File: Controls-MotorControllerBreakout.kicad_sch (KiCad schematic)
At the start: 12 parts, among them J1 MC CAN 1, J2 MC CAN 2, J3 Controls CAN, J4 CANdapter, J5 Ext. PWR

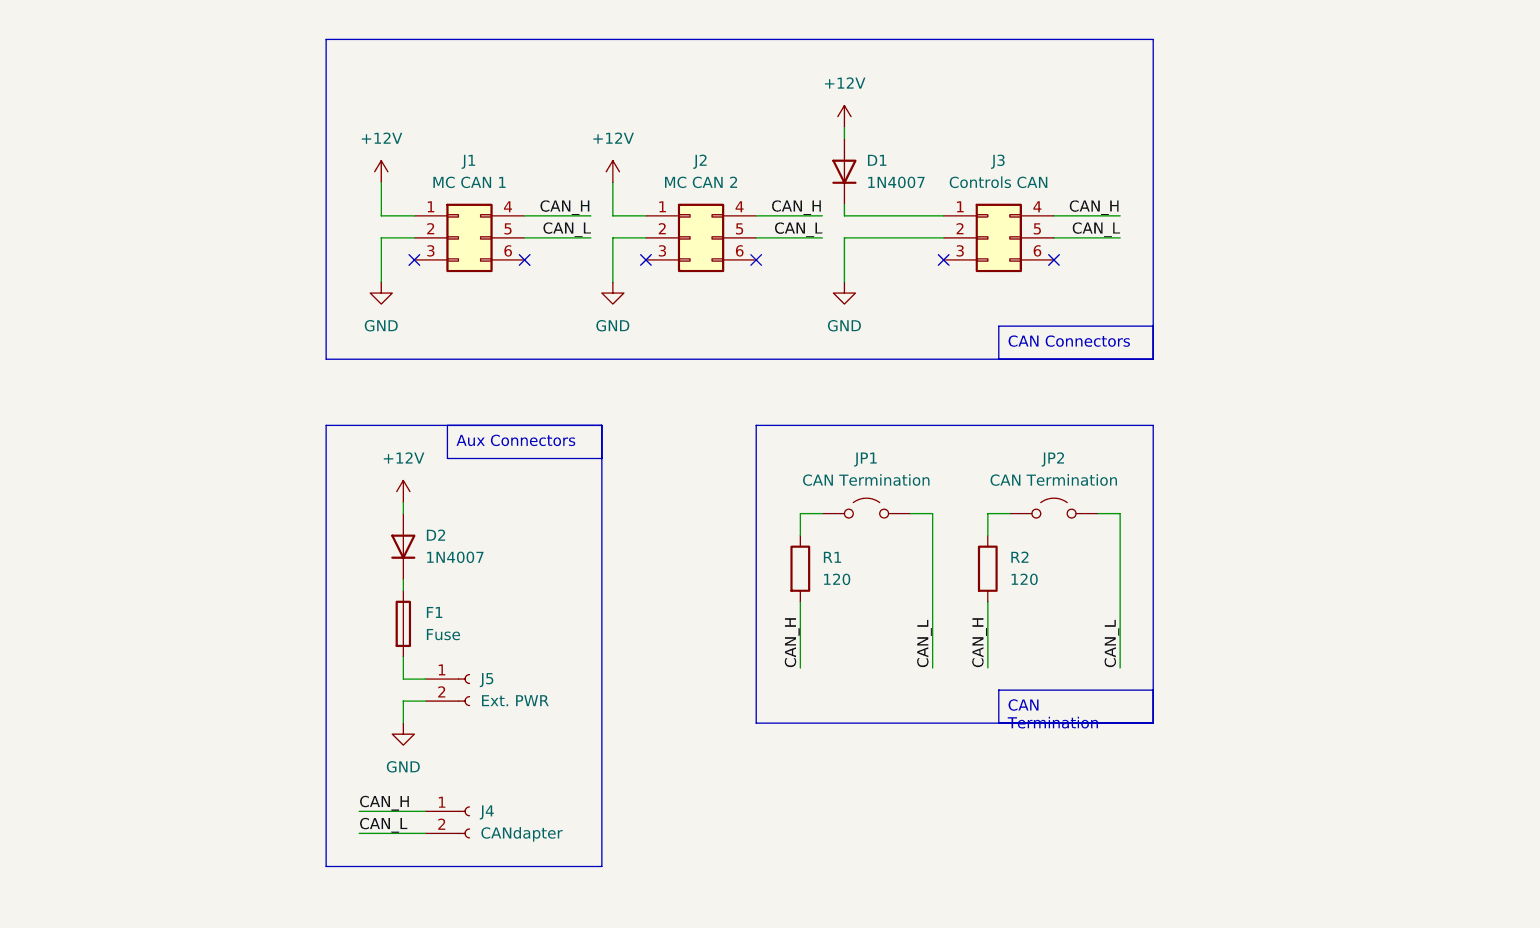
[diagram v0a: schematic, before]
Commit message: add alternative controls conn
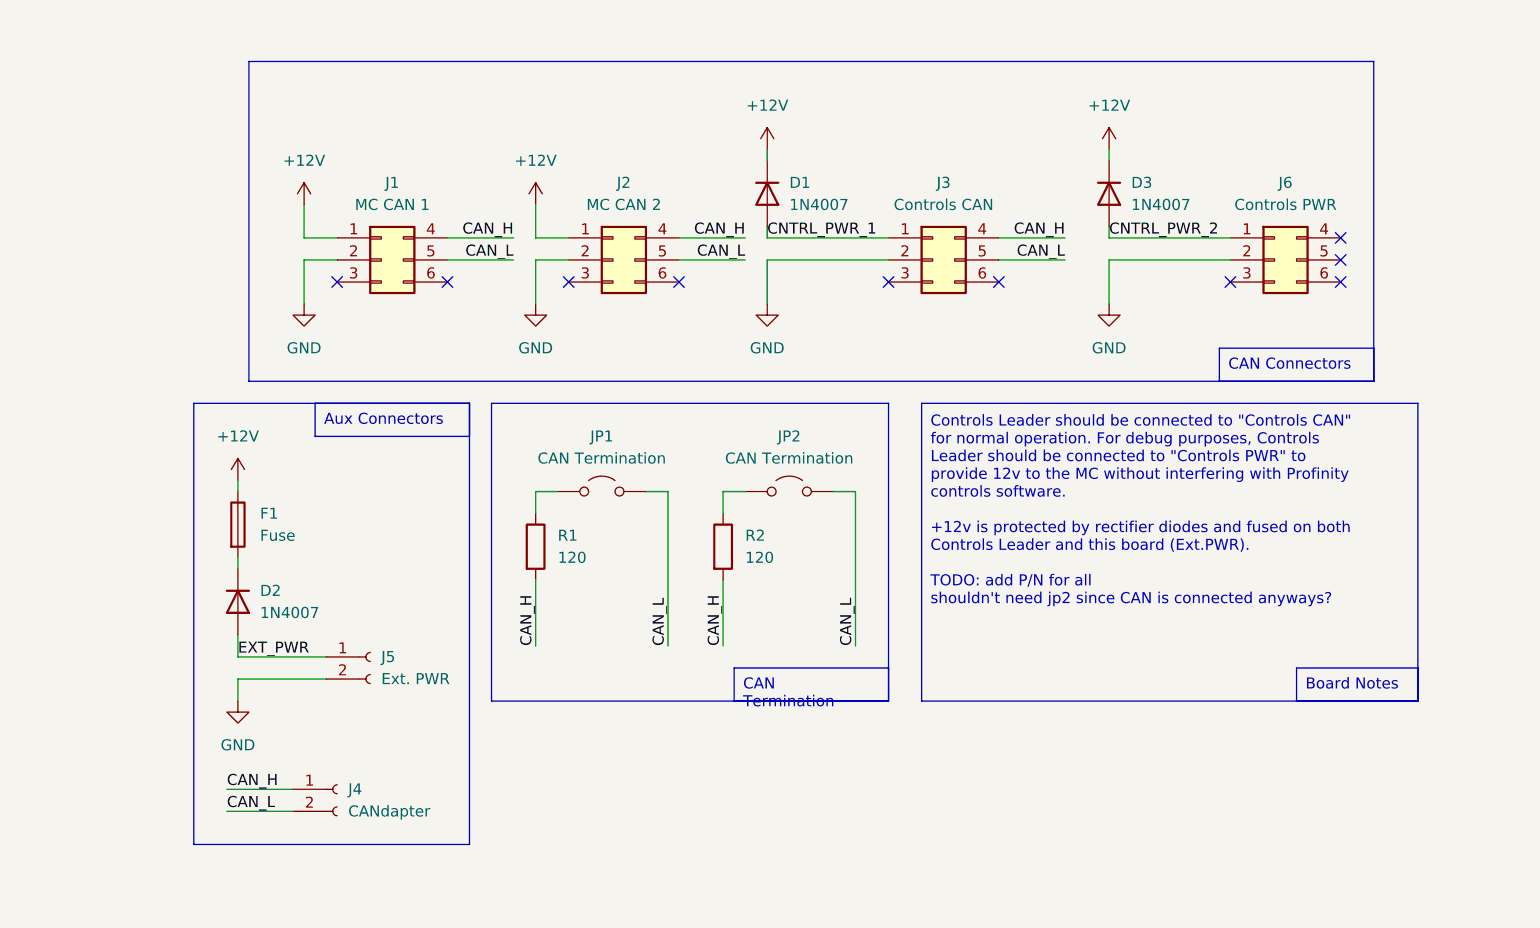
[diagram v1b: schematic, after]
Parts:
- added D3: 1N4007, Diode_SMD:D_SOD-123F, symbol Device:D
- added J6: Controls PWR, Connector_Molex:Molex_Micro-Fit_3.0_43045-0612_2x03_P3.00mm_Vertical, symbol Connector_Generic:Conn_02x03_Top_Bottom
- D1, D2: footprint (none) -> Diode_SMD:D_SOD-123F
- J1, J2, J3: footprint (none) -> Connector_Molex:Molex_Micro-Fit_3.0_43045-0612_2x03_P3.00mm_Vertical
- J4, J5: footprint (none) -> Connector_Molex:Molex_Micro-Fit_3.0_43650-0215_1x02_P3.00mm_Vertical
- JP1, JP2: footprint (none) -> Connector_PinHeader_2.54mm:PinHeader_1x02_P2.54mm_Vertical
- R1, R2: footprint (none) -> Resistor_SMD:R_0805_2012Metric
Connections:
- net +12V: now also D1.1 (K), F1.1, D3.1 (K); no longer D1.2 (A), D2.2 (A)
- net GND: now also J6.2 (Pin_2)
- net at D2.1 (K): now also F1.2; no longer F1.1
- net EXT_PWR: now reaches J5.1 (Pin_1)
- net EXT_PWR: now also D2.2 (A); no longer F1.2
- net CNTRL_PWR_1: now reaches J3.1 (Pin_1)
- net CNTRL_PWR_1: now also D1.2 (A); no longer D1.1 (K)
- new net CNTRL_PWR_2: D3.2 (A), J6.1 (Pin_1)
- no-connect marks 6 -> 10
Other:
- note added: "Controls Leader should be connected to "Controls CAN" for normal operation. For debug purposes, Controls Leader should be connected to "Controls PWR" to provide 12v to the MC without interfering with Profinity controls software. +12v is protected by rectifier diodes and fused on both Controls Leader and this board (Ext.PWR). TODO: add P/N for all shouldn't need jp2 since CAN is connected anyways?"
- moved on the sheet: D1, J1, J2, J3, J4, J5, JP1, JP2, R1, R2

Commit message: decouple pwr from can
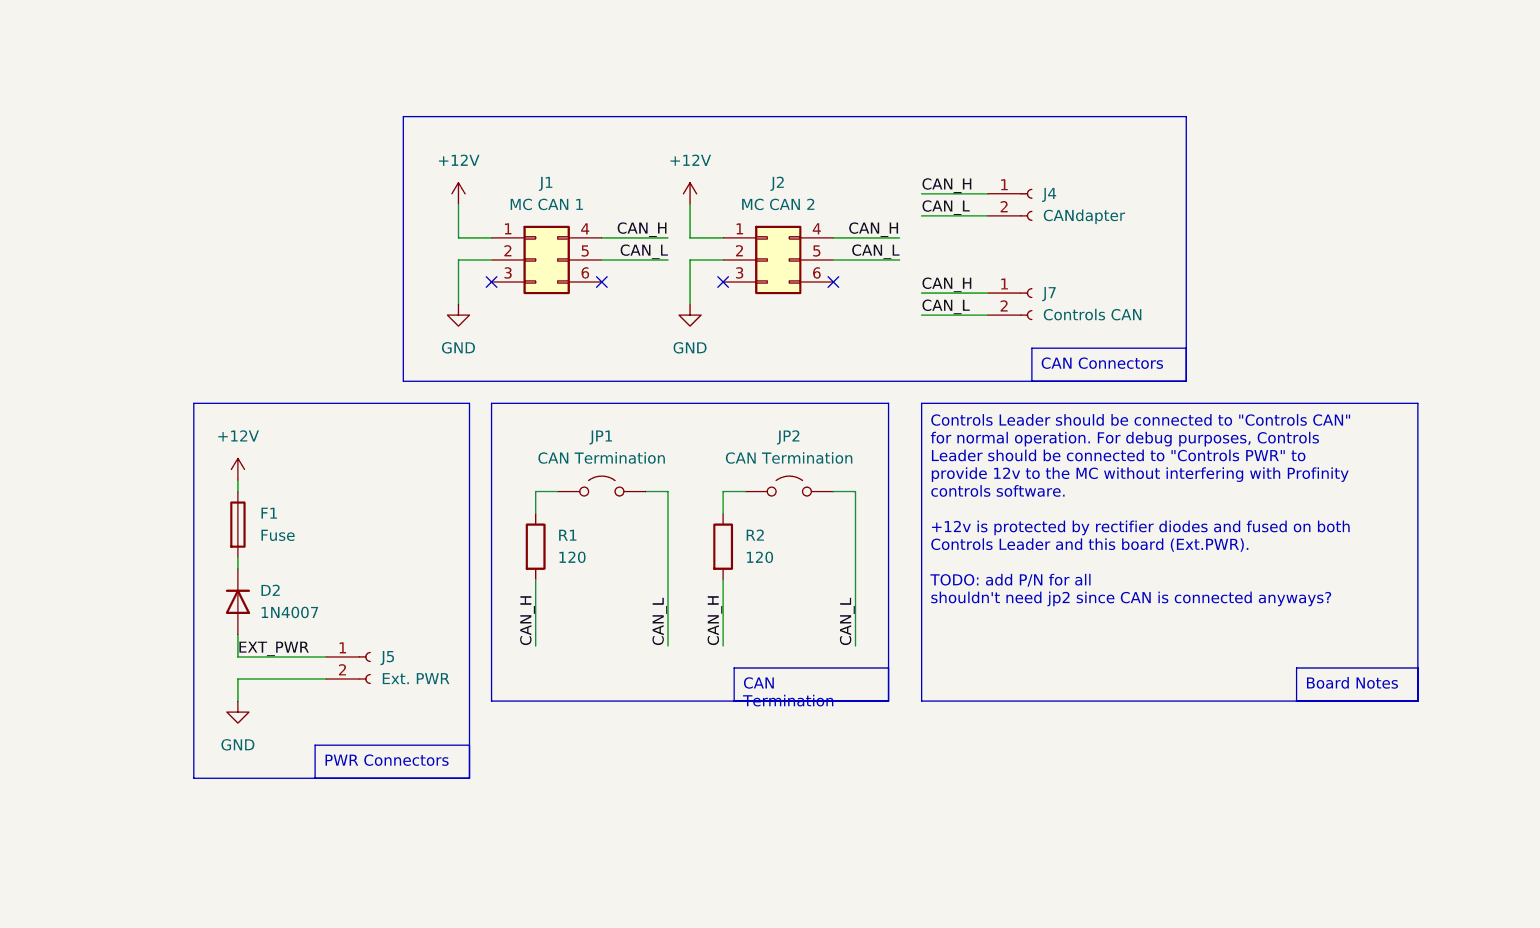
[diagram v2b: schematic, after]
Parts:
- removed D1, D3: 1N4007, Diode_SMD:D_SOD-123F, symbol Device:D
- removed J3: Controls CAN, Connector_Molex:Molex_Micro-Fit_3.0_43045-0612_2x03_P3.00mm_Vertical, symbol Connector_Generic:Conn_02x03_Top_Bottom
- removed J6: Controls PWR, Connector_Molex:Molex_Micro-Fit_3.0_43045-0612_2x03_P3.00mm_Vertical, symbol Connector_Generic:Conn_02x03_Top_Bottom
- added J7: Controls CAN, Connector_Molex:Molex_Micro-Fit_3.0_43650-0215_1x02_P3.00mm_Vertical, symbol Connector:Conn_01x02_Socket
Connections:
- net CAN_H: now also J7.1 (Pin_1)
- net CAN_L: now also J7.2 (Pin_2)
- no-connect marks 10 -> 4
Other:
- moved on the sheet: J1, J2

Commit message: pwr led and rm second term resistors
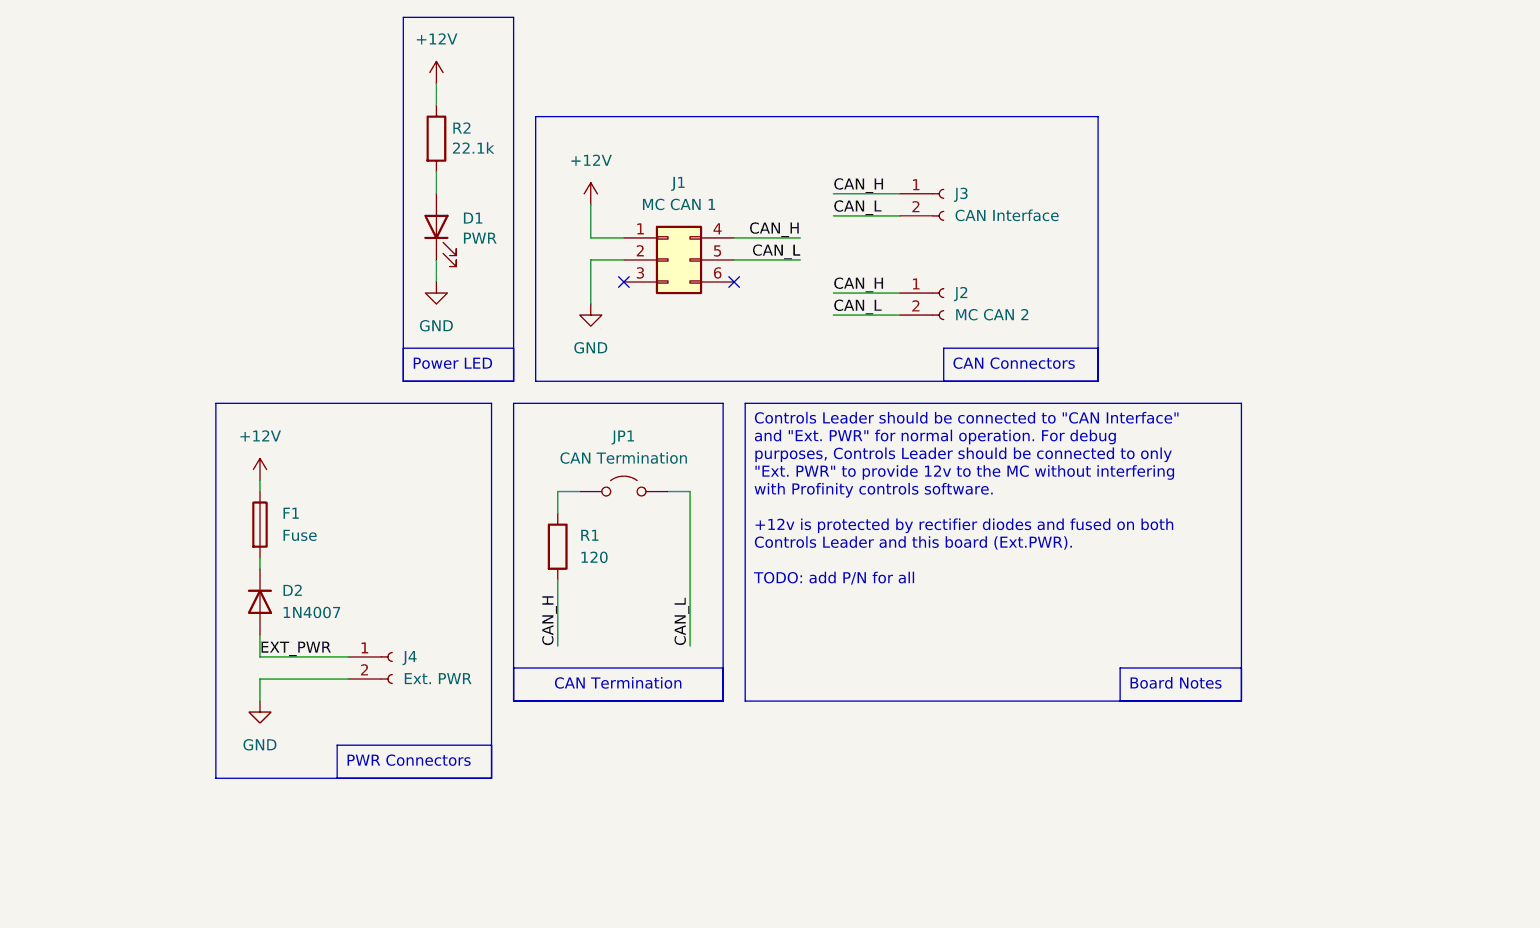
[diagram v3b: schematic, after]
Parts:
- removed J2: MC CAN 2, Connector_Molex:Molex_Micro-Fit_3.0_43045-0612_2x03_P3.00mm_Vertical, symbol Connector_Generic:Conn_02x03_Top_Bottom
- removed JP2: CAN Termination, Connector_PinHeader_2.54mm:PinHeader_1x02_P2.54mm_Vertical, symbol Jumper:Jumper_2_Open
- added D1: PWR, LED_SMD:LED_0805_2012Metric, symbol Device:LED
- J2: renamed from J7; value Controls CAN -> MC CAN 2
- J3: renamed from J4; value CANdapter -> CAN Interface
- R2: value 120 -> 22.1k; Inventory (none) -> Y; Mouser Part Number (none) -> 71-CRCW0805-22.1K-E3; Mouser Price/Stock (none) -> https://www.mouser.com/ProductDetail/Vishay-Dale/CRCW080522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; P/N (none) -> CRCW080522K1FKEA
- renumbered J5 to J4
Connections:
- net +12V: now also R2.1
- net CAN_H: no longer R2.2
- net GND: now also D1.1 (K)
- new net: D1.2 (A), R2.2
- no-connect marks 4 -> 2
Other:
- note added: "Controls Leader should be connected to "CAN Interface" and "Ext. PWR" for normal operation. For debug purposes, Controls Leader should be connected to only "Ext. PWR" to provide 12v to the MC without interfering with Profinity controls software. +12v is protected by rectifier diodes and fused on both Controls Leader and this board (Ext.PWR). TODO: add P/N for all"
- note removed: "Controls Leader should be connected to "Controls CAN" for normal operation. For debug purposes, Controls Leader should be connected to "Controls PWR" to provide 12v to the MC without interfering with Profinity controls software. +12v is protected by rectifier diodes and fused on both Controls Leader and this board (Ext.PWR). TODO: add P/N for all shouldn't need jp2 since CAN is connected anyways?"
- moved on the sheet: D2, F1, J1, J2, J3, J4, JP1, R1

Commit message: initial layout/routing
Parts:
- added H1, H2, H3, H4: M3, MountingHole:MountingHole_3mm, symbol Mechanical:MountingHole
- added LOGO1: UTSVT Logo, UTSVT_Special:UTSVT_Logo_Symbol, symbol utsvt-misc:Logo_Placeholder
- J3: value CAN Interface -> CAN INTRFC
- J4: value Ext. PWR -> EXT PWR
- JP1: value CAN Termination -> CAN TERM
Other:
- note added: "Controls Leader should be connected to "CAN INTRFC" and "EXT PWR" for normal operation. For debug purposes, Controls Leader should be connected to only "EXT PWR" to provide 12v to the MC without interfering with Profinity controls software. +12v is protected by rectifier diodes and fused on both Controls Leader and this board (EXT PWR). TODO: add P/N for all"
- note removed: "Controls Leader should be connected to "CAN Interface" and "Ext. PWR" for normal operation. For debug purposes, Controls Leader should be connected to only "Ext. PWR" to provide 12v to the MC without interfering with Profinity controls software. +12v is protected by rectifier diodes and fused on both Controls Leader and this board (Ext.PWR). TODO: add P/N for all"

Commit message: part numbers
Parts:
- F1: P/N (none) -> 576-0440.375WR
- J1: P/N (none) -> 430450612
- J2, J3, J4: P/N (none) -> 0436500215
- R1: P/N (none) -> CRCW0805120RFKEA
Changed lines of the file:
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@@
+	)
+	(rectangle
+		(start 140.97 27.94)
+		(end 165.1 58.42)
+		(stroke
+			(width 0)
+			(type default)
+		)
+		(fill
+			(type none)
+		)
 	)
 	(rectangle
@@
 		)
 	)
+	(text_box "Graphics"
+		(exclude_from_sim no)
+		(at 154.94 54.61 0)
+		(size 10.16 3.81)
+		(stroke
+			(width 0)
+			(type default)
+		)
+		(fill
+			(type none)
+		)
+		(effects
+			(font
+				(size 1.27 1.27)
+			)
+			(justify left top)
+		)
+	)
 	(text_box "Board Notes"
 		(exclude_from_sim no)
@@
 			)
 		)
+		(property "P/N" "430450612"
+			(at 88.9 44.45 0)
+			(effects
+				(font
+					(size 1.27 1.27)
+				)
+				(hide yes)
+			)
+		)
 		(pin "1"
 		)
@@
 			)
 		)
-		(property "Datasheet" "~"
+		(property "Datasheet" "https://www.mouser.com/ProductDetail/71-CRCW0805-22.1K-E3"
 			(at 62.23 30.48 0)
 			(effects
@@
 			)
 		)
+		(property "P/N" "576-0440.375WR "
+			(at 41.91 74.93 0)
+			(effects
+				(font
+					(size 1.27 1.27)
+				)
+				(hide yes)
+			)
+		)
 		(pin "2"
 		)
@@
 			)
 		)
+		(property "P/N" "0436500215"
+			(at 57.15 90.17 0)
+			(effects
+				(font
+					(size 1.27 1.27)
+				)
+				(hide yes)
+			)
+		)
 		(pin "1"
 		)
@@
 			)
 		)
+		(property "P/N" "0436500215"
+			(at 120.65 48.26 0)
+			(effects
+				(font
+					(size 1.27 1.27)
+				)
+				(hide yes)
+			)
+		)
 		(pin "1"
 		)
@@
 			)
 		)
+		(property "P/N" "0436500215"
+			(at 120.65 36.83 0)
+			(effects
+				(font
+					(size 1.27 1.27)
+				)
+				(hide yes)
+			)
+		)
 		(pin "1"
 		)
@@
 			)
 		)
-		(property "Datasheet" "~"
+		(property "Datasheet" "https://www.mouser.com/ProductDetail/71-CRCW0805120RFKEA"
 			(at 76.2 77.47 0)
 			(effects
@@
 			(at 76.2 77.47 0)
 			(effects
+				(font
+					(size 1.27 1.27)
+				)
+				(hide yes)
+			)
+		)
+		(property "P/N" "CRCW0805120RFKEA"
+			(at 76.2 77.47 0)
+			(effects

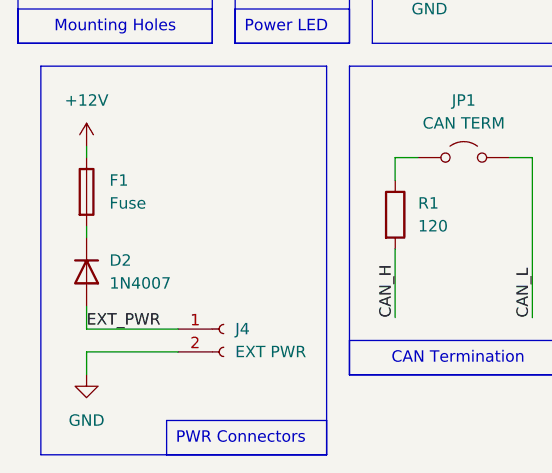
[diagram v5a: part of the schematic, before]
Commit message: change diode + models
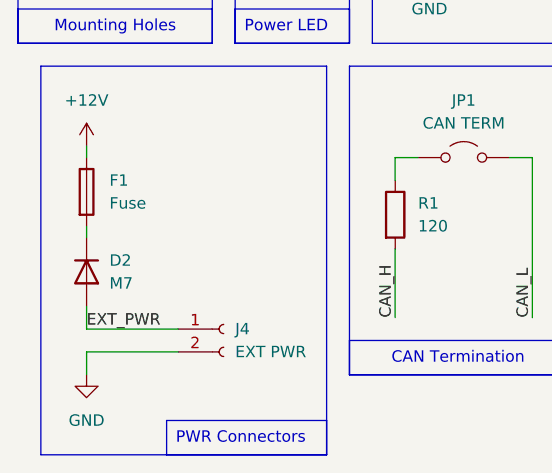
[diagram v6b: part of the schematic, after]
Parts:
- D2: value 1N4007 -> M7; P/N 1N4007FL -> RS1MWF-7
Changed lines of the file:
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@@
 			)
 		)
-		(property "Value" "1N4007"
+		(property "Value" "M7"
 			(at 44.45 85.0899 90)
 			(effects
@@
 			)
 		)
-		(property "Datasheet" "https://www.digikey.com/en/products/detail/smc-diode-solutions/1N4007FL/11657817"
+		(property "Datasheet" "https://www.diodes.com/assets/Datasheets/RS1MWF.pdf"
 			(at 41.91 83.82 0)
 			(effects
@@
 			)
 		)
-		(property "P/N" "1N4007FL"
+		(property "P/N" "RS1MWF-7"
 			(at 41.91 83.82 90)
 			(effects
